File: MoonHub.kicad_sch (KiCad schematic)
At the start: 33 parts, among them J1 USB_A, J2 USB_C_Receptacle_USB2.0, J3 USB_C_Receptacle_USB2.0, J4 USB_A, U1 SRV05-4, U2 SRV05-4, U3 CH334U, U4 TPS2552DBVR, Y1 12MHz

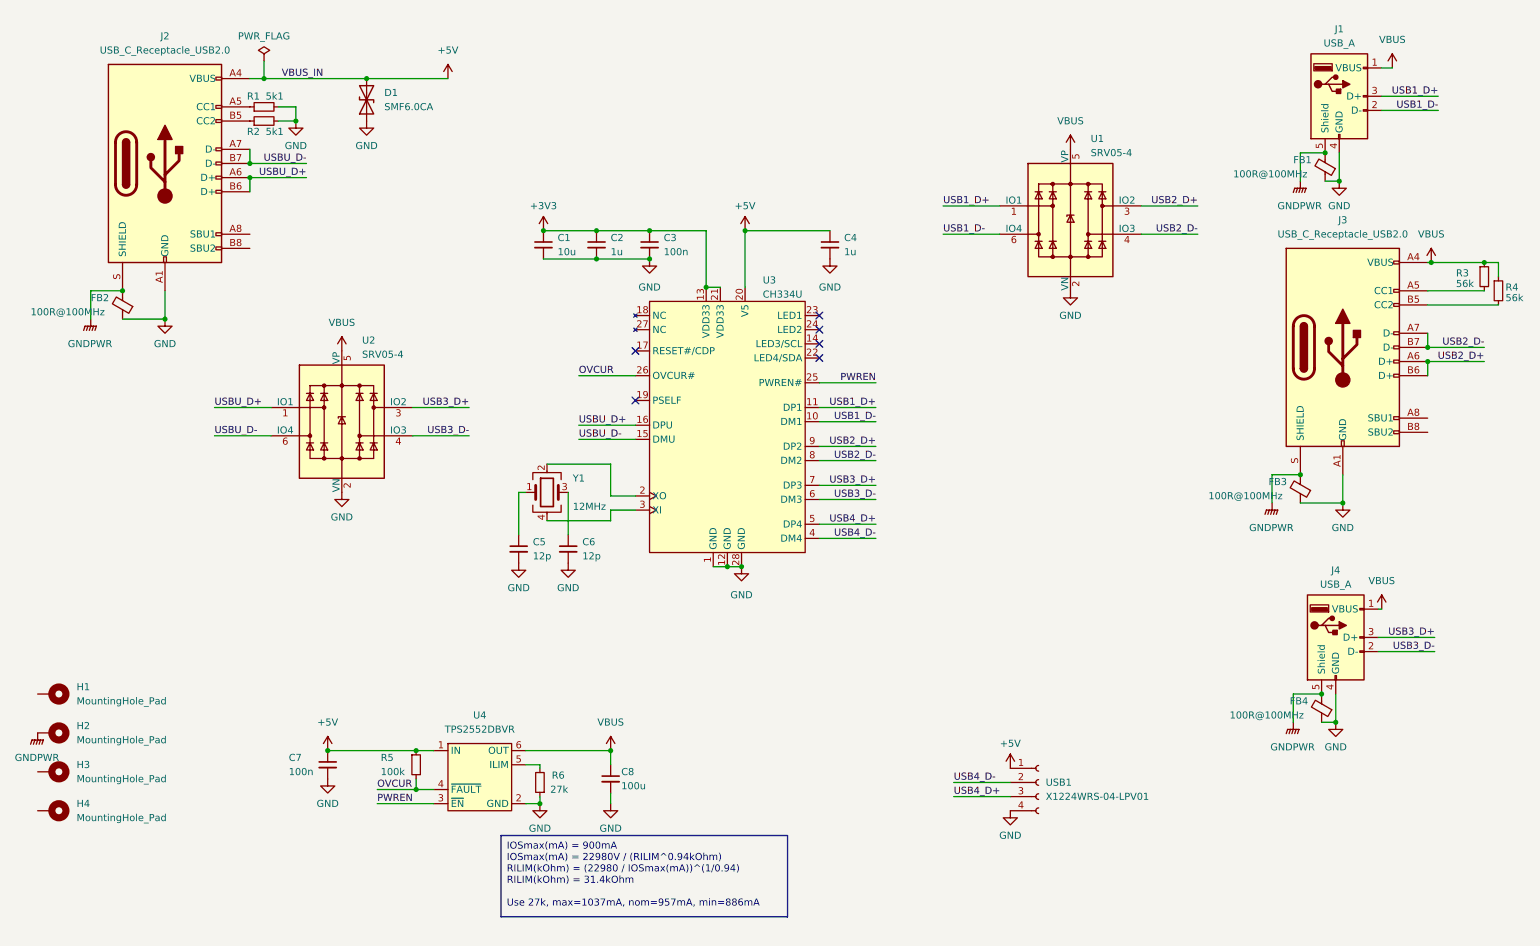
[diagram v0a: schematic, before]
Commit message: fully routed
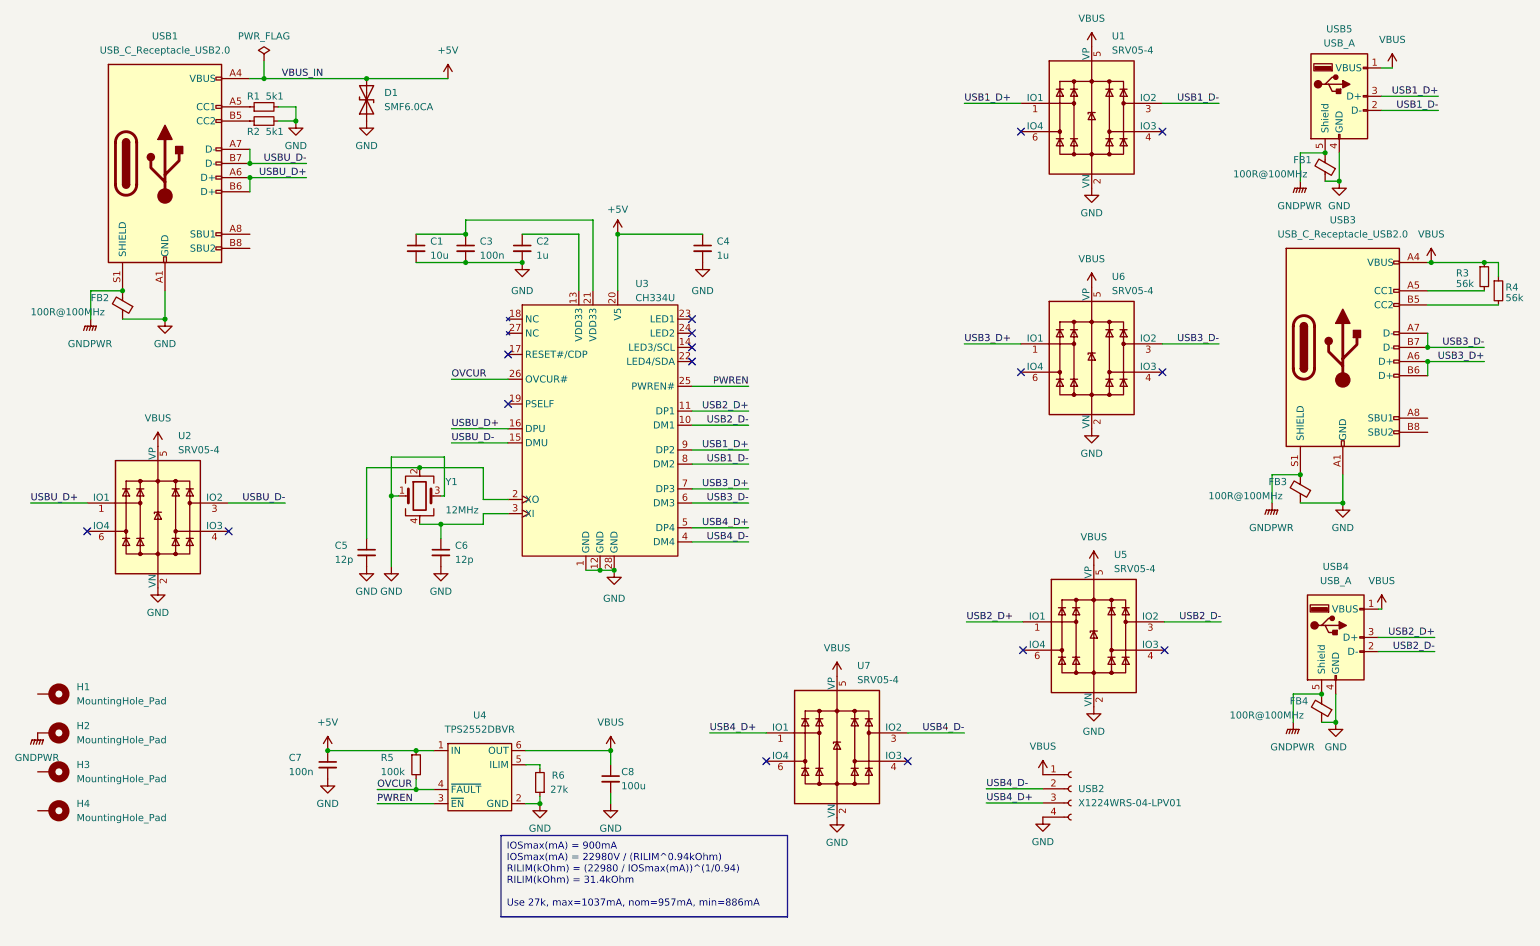
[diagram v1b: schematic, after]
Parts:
- added U5, U6, U7: SRV05-4, PCM_marbastlib-various:SOT-23-6-routable, symbol PCM_marbastlib-various:SRV05-4
- USB1: renamed from J2; footprint MoonHub:TYPE-C-31-M-12 -> MoonHub:HRO-TYPE-C-31-M-12-Assembly
- USB2: renamed from USB1; footprint MoonHub:PicoEZMate-Reinforced-Alt -> MoonHub:PicoEZMate-Reinforced-Lite
- USB3: renamed from J3; footprint MoonHub:TYPE-C-31-M-12 -> MoonHub:HRO-TYPE-C-31-M-12-Assembly
- USB4: renamed from J4; footprint MoonHub:USB-A-SMD_AF-APPLE-10.6 -> MoonHub:USB-A-SMD_USB-M-21_914-441A2021S10200
- USB5: renamed from J1; footprint MoonHub:USB-A-SMD_AF-APPLE-10.6 -> MoonHub:USB-A-SMD_USB-M-21_914-441A2021S10200
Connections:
- net +5V: no longer USB2.1 (Pin_1)
- net GND: now also Y1.1, Y1.3, U5.2 (VN), U6.2 (VN), U7.2 (VN)
- net GNDPWR: now also USB1.S1 (SHIELD), USB3.S1 (SHIELD); no longer USB1.S (SHIELD), USB3.S (SHIELD)
- net USB1_D+: now also U3.9 (DP2); no longer U3.11 (DP1)
- net USB1_D-: now also U1.3 (IO2), U3.8 (DM2); no longer U1.6 (IO4), U3.10 (DM1)
- net USB2_D+: now also U3.11 (DP1), USB4.3 (D+), U5.1 (IO1); no longer U1.3 (IO2), U3.9 (DP2), USB3.A6 (D+), USB3.B6 (D+)
- net USB2_D-: now also U3.10 (DM1), USB4.2 (D-), U5.3 (IO2); no longer U1.4 (IO3), U3.8 (DM2), USB3.A7 (D-), USB3.B7 (D-)
- net USB3_D+: now also USB3.A6 (D+), USB3.B6 (D+), U6.1 (IO1); no longer U2.3 (IO2), USB4.3 (D+)
- net USB3_D-: now also USB3.A7 (D-), USB3.B7 (D-), U6.3 (IO2); no longer U2.4 (IO3), USB4.2 (D-)
- net USB4_D+: now also U7.1 (IO1)
- net USB4_D-: now also U7.3 (IO2)
- net USBU_D-: now also U2.3 (IO2); no longer U2.6 (IO4)
- net VBUS: now also USB2.1 (Pin_1), U5.5 (VP), U6.5 (VP), U7.5 (VP)
- net at C5.1: now also U3.2 (XO), Y1.2; no longer Y1.1
- net at C6.1: now also U3.3 (XI), Y1.4; no longer Y1.3
- net +3V3: no longer names the net of C1.1, C3.1, U3.21 (VDD33)
- net +3V3: no longer C2.1, U3.13 (VDD33)
- new net: C2.1, U3.13 (VDD33)
- no-connect marks 6 -> 16
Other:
- moved on the sheet: C1, C2, C3, C4, C5, C6, U1, U2, U3, USB2, Y1

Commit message: reroute for smaller size
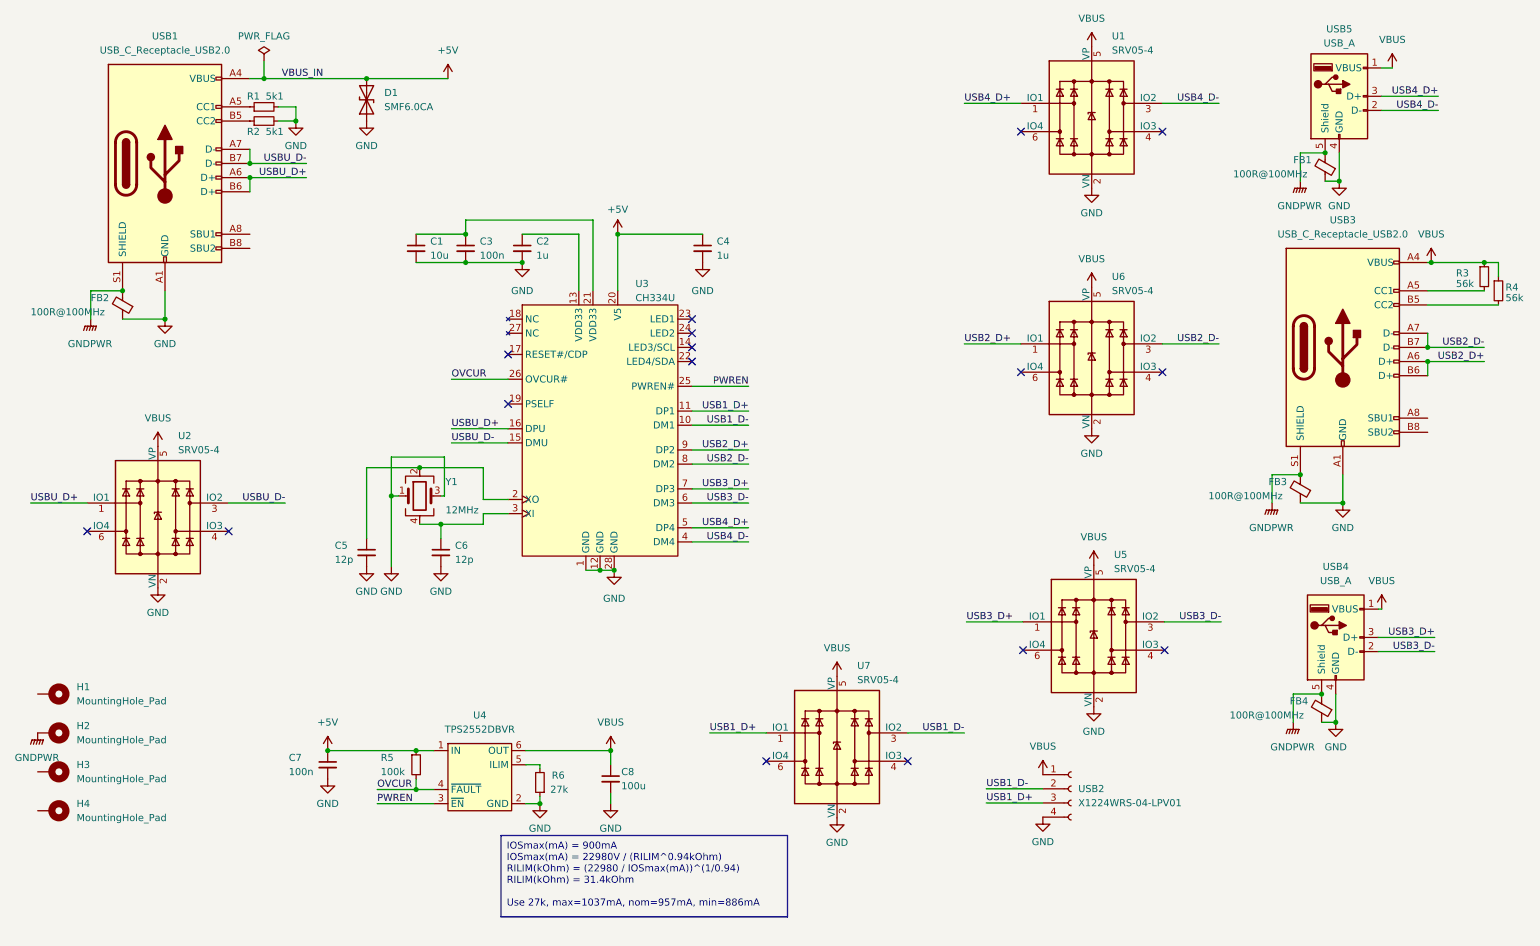
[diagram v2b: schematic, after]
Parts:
- C3, C7: footprint Capacitor_SMD:C_0402_1005Metric -> Capacitor_SMD:C_0805_2012Metric
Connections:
- net USB1_D+: now also U3.11 (DP1), U7.1 (IO1), USB2.3 (Pin_3); no longer U1.1 (IO1), U3.9 (DP2), USB5.3 (D+)
- net USB1_D-: now also U3.10 (DM1), U7.3 (IO2), USB2.2 (Pin_2); no longer U1.3 (IO2), U3.8 (DM2), USB5.2 (D-)
- net USB2_D+: now also U3.9 (DP2), U6.1 (IO1), USB3.A6 (D+), USB3.B6 (D+); no longer U3.11 (DP1), U5.1 (IO1), USB4.3 (D+)
- net USB2_D-: now also U3.8 (DM2), U6.3 (IO2), USB3.A7 (D-), USB3.B7 (D-); no longer U3.10 (DM1), U5.3 (IO2), USB4.2 (D-)
- net USB3_D+: now also U5.1 (IO1), USB4.3 (D+); no longer U6.1 (IO1), USB3.A6 (D+), USB3.B6 (D+)
- net USB3_D-: now also U5.3 (IO2), USB4.2 (D-); no longer U6.3 (IO2), USB3.A7 (D-), USB3.B7 (D-)
- net USB4_D+: now also U1.1 (IO1), USB5.3 (D+); no longer U7.1 (IO1), USB2.3 (Pin_3)
- net USB4_D-: now also U1.3 (IO2), USB5.2 (D-); no longer U7.3 (IO2), USB2.2 (Pin_2)
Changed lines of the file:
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@@
   (no_connect (at 192.405 36.195))
   (no_connect (at 133.35 72.39))
+  (no_connect (at 133.35 77.47))
   (no_connect (at 50.165 107.95))
   (no_connect (at 100.33 76.2))
-  (no_connect (at 133.35 77.47))
   (no_connect (at 217.805 79.375))
   (no_connect (at 192.786 129.286))
+  (no_connect (at 133.35 69.85))
   (no_connect (at 24.765 107.95))
   (no_connect (at 192.405 79.375))
@@
   (no_connect (at 218.186 129.286))
   (no_connect (at 146.685 149.225))
-  (no_connect (at 133.35 69.85))
   (no_connect (at 133.35 74.93))
   (wire (pts (xy 275.59 77.47) (xy 265.43 77.47))
     (stroke (width 0) (type default))
   )
-  (wire (pts (xy 116.84 114.935) (xy 119.38 114.935))
+  (wire (pts (xy 136.525 144.145) (xy 146.685 144.145))
     (stroke (width 0) (type default))
   )
-  (wire (pts (xy 100.33 104.775) (xy 95.885 104.775))
+  (wire (pts (xy 116.84 114.935) (xy 119.38 114.935))
     (stroke (width 0) (type default))
   )
-  (wire (pts (xy 136.525 144.145) (xy 146.685 144.145))
+  (wire (pts (xy 100.33 104.775) (xy 95.885 104.775))
     (stroke (width 0) (type default))
   )
@@
     (stroke (width 0) (type default))
   )
-  (wire (pts (xy 182.245 144.145) (xy 172.085 144.145))
-    (stroke (width 0) (type default))
-  )
   (wire (pts (xy 56.515 23.495) (xy 56.515 26.67))
     (stroke (width 0) (type default))
@@
     (stroke (width 0) (type default))
   )
+  (wire (pts (xy 182.245 144.145) (xy 172.085 144.145))
+    (stroke (width 0) (type default))
+  )
   (wire (pts (xy 266.7 127) (xy 256.54 127))
     (stroke (width 0) (type default))
@@
     (stroke (width 0) (type default))
   )
-  (wire (pts (xy 143.51 88.9) (xy 133.35 88.9))
+  (wire (pts (xy 143.51 95.885) (xy 133.35 95.885))
     (stroke (width 0) (type default))
   )
@@
     (stroke (width 0) (type default))
   )
-  (wire (pts (xy 143.51 95.885) (xy 133.35 95.885))
+  (wire (pts (xy 143.51 88.9) (xy 133.35 88.9))
     (stroke (width 0) (type default))
   )
@@
     (stroke (width 0) (type default))
   )
-  (wire (pts (xy 143.51 86.36) (xy 133.35 86.36))
+  (wire (pts (xy 143.51 93.345) (xy 133.35 93.345))
     (stroke (width 0) (type default))
   )
@@
     (stroke (width 0) (type default))
   )
-  (wire (pts (xy 143.51 93.345) (xy 133.35 93.345))
+  (wire (pts (xy 143.51 86.36) (xy 133.35 86.36))
     (stroke (width 0) (type default))
   )
@@
     (effects (font (size 1.27 1.27)) (justify left top))
   )
+  (label "USB1_D-" (at 182.245 144.145 180) (fields_autoplaced)
+    (effects (font (size 1.27 1.27)) (justify right bottom))
+  )
   (label "USBU_D-" (at 60.325 102.87 180) (fields_autoplaced)
     (effects (font (size 1.27 1.27)) (justify right bottom))
   )
-  (label "USB2_D+" (at 143.51 86.36 180) (fields_autoplaced)
+  (label "USB2_D+" (at 143.51 93.345 180) (fields_autoplaced)
     (effects (font (size 1.27 1.27)) (justify right bottom))
   )
@@
     (effects (font (size 1.27 1.27)) (justify right bottom))
   )
-  (label "USB1_D+" (at 182.245 31.115 0) (fields_autoplaced)
+  (label "USB4_D+" (at 182.245 31.115 0) (fields_autoplaced)
     (effects (font (size 1.27 1.27)) (justify left bottom))
   )
@@
     (effects (font (size 1.27 1.27)) (justify right bottom))
   )
-  (label "USB2_D+" (at 182.626 124.206 0) (fields_autoplaced)
+  (label "USB3_D+" (at 182.626 124.206 0) (fields_autoplaced)
     (effects (font (size 1.27 1.27)) (justify left bottom))
   )
@@
     (effects (font (size 1.27 1.27)) (justify left bottom))
   )
-  (label "USB1_D-" (at 227.965 31.115 180) (fields_autoplaced)
+  (label "USB4_D-" (at 227.965 31.115 180) (fields_autoplaced)
     (effects (font (size 1.27 1.27)) (justify right bottom))
   )
-  (label "USB2_D+" (at 266.7 127 180) (fields_autoplaced)
+  (label "USB3_D+" (at 266.7 127 180) (fields_autoplaced)
     (effects (font (size 1.27 1.27)) (justify right bottom))
   )
-  (label "USB2_D-" (at 143.51 88.9 180) (fields_autoplaced)
+  (label "USB2_D-" (at 143.51 95.885 180) (fields_autoplaced)
     (effects (font (size 1.27 1.27)) (justify right bottom))
   )
@@
     (effects (font (size 1.27 1.27)) (justify left bottom))
   )
-  (label "USB4_D-" (at 182.245 144.145 180) (fields_autoplaced)
-    (effects (font (size 1.27 1.27)) (justify right bottom))
+  (label "USB1_D+" (at 136.525 144.145 0) (fields_autoplaced)
+    (effects (font (size 1.27 1.27)) (justify left bottom))
   )
   (label "USB4_D+" (at 143.51 107.315 180) (fields_autoplaced)
     (effects (font (size 1.27 1.27)) (justify right bottom))
   )
-  (label "USB2_D-" (at 266.7 129.54 180) (fields_autoplaced)
+  (label "USB3_D-" (at 266.7 129.54 180) (fields_autoplaced)
     (effects (font (size 1.27 1.27)) (justify right bottom))
   )
-  (label "USB4_D-" (at 186.182 154.178 0) (fields_autoplaced)
+  (label "USB1_D-" (at 186.182 154.178 0) (fields_autoplaced)
     (effects (font (size 1.27 1.27)) (justify left bottom))
   )
-  (label "USB4_D+" (at 186.182 156.718 0) (fields_autoplaced)
+  (label "USB1_D+" (at 186.182 156.718 0) (fields_autoplaced)
     (effects (font (size 1.27 1.27)) (justify left bottom))
   )
-  (label "USB2_D-" (at 228.346 124.206 180) (fields_autoplaced)
+  (label "USB3_D-" (at 228.346 124.206 180) (fields_autoplaced)
     (effects (font (size 1.27 1.27)) (justify right bottom))
   )
-  (label "USB3_D-" (at 275.59 74.93 180) (fields_autoplaced)
+  (label "USB2_D-" (at 275.59 74.93 180) (fields_autoplaced)
     (effects (font (size 1.27 1.27)) (justify right bottom))
   )
@@
     (effects (font (size 1.27 1.27)) (justify right bottom))
   )
-  (label "USB1_D-" (at 267.335 32.385 180) (fields_autoplaced)
+  (label "USB4_D-" (at 267.335 32.385 180) (fields_autoplaced)
     (effects (font (size 1.27 1.27)) (justify right bottom))
   )
-  (label "USB1_D+" (at 267.335 29.845 180) (fields_autoplaced)
+  (label "USB4_D+" (at 267.335 29.845 180) (fields_autoplaced)
     (effects (font (size 1.27 1.27)) (justify right bottom))
   )
-  (label "USB1_D+" (at 143.51 93.345 180) (fields_autoplaced)
+  (label "USB1_D+" (at 143.51 86.36 180) (fields_autoplaced)
     (effects (font (size 1.27 1.27)) (justify right bottom))
   )
@@
     (effects (font (size 1.27 1.27)) (justify left bottom))
   )
-  (label "USB1_D-" (at 143.51 95.885 180) (fields_autoplaced)
+  (label "USB1_D-" (at 143.51 88.9 180) (fields_autoplaced)
     (effects (font (size 1.27 1.27)) (justify right bottom))
   )
@@
     (effects (font (size 1.27 1.27)) (justify left bottom))
   )
-  (label "USB3_D+" (at 275.59 77.47 180) (fields_autoplaced)
+  (label "USB2_D+" (at 275.59 77.47 180) (fields_autoplaced)
     (effects (font (size 1.27 1.27)) (justify right bottom))
   )
-  (label "USB4_D+" (at 136.525 144.145 0) (fields_autoplaced)
-    (effects (font (size 1.27 1.27)) (justify left bottom))
-  )
-  (label "USB3_D+" (at 182.245 74.295 0) (fields_autoplaced)
+  (label "USB2_D+" (at 182.245 74.295 0) (fields_autoplaced)
     (effects (font (size 1.27 1.27)) (justify left bottom))
   )
@@
     (effects (font (size 1.27 1.27)) (justify left bottom))
   )
-  (label "USB3_D-" (at 227.965 74.295 180) (fields_autoplaced)
+  (label "USB2_D-" (at 227.965 74.295 180) (fields_autoplaced)
     (effects (font (size 1.27 1.27)) (justify right bottom))
   )
@@
       (effects (font (size 1.27 1.27)) (justify left))
     )
-    (property "Footprint" "Capacitor_SMD:C_0402_1005Metric" (at 92.71 57.15 0)
+    (property "Footprint" "Capacitor_SMD:C_0805_2012Metric" (at 92.71 57.15 0)
       (effects (font (size 1.27 1.27)) hide)
     )
@@
       (effects (font (size 1.27 1.27)) (justify left))
     )
-    (property "Footprint" "Capacitor_SMD:C_0402_1005Metric" (at 67.945 149.86 0)
+    (property "Footprint" "Capacitor_SMD:C_0805_2012Metric" (at 67.945 149.86 0)
       (effects (font (size 1.27 1.27)) hide)
     )
